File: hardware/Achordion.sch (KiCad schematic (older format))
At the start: 96 parts, among them J1 Power, J10 Jack, J11 Jack, J4 Jack, J5 Jack, J6 Jack, J7 Jack, J8 Jack, J9 Jack, SW2 Button, U4 LM4040C10, U6 TL072, U7 MCP6002, U8 MCP6002, U9 MCP6002

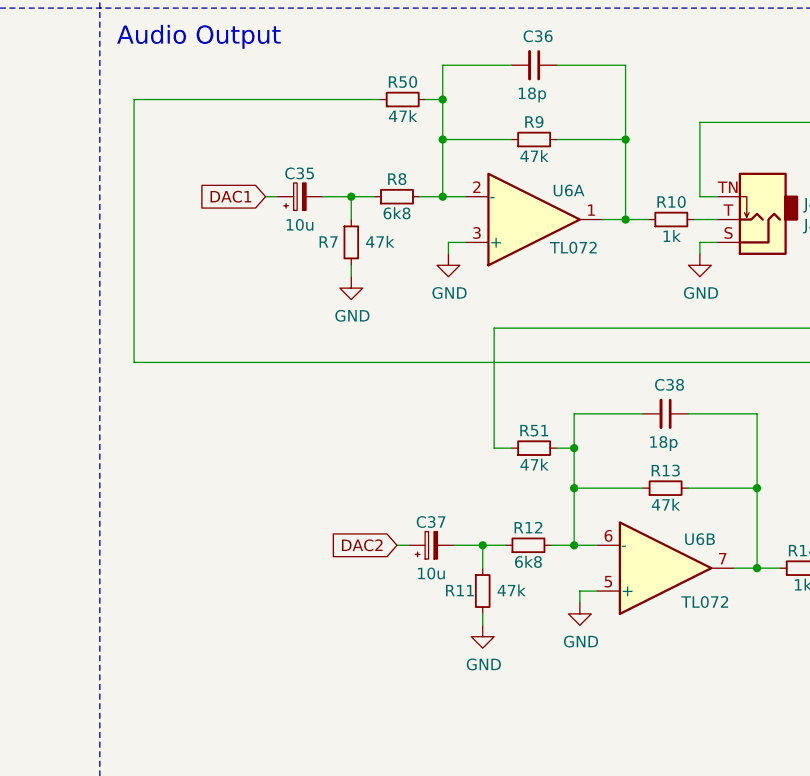
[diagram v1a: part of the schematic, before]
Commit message: Replace DAC decoupling cap with LPF
The design with big decoupling cap was taken from WM8731 used for
Elements. However, with AK4556 used in Daisy Seed, it is not needed (or
at least not a part of the datasheet), instead, use LPF for ~70 kHz.

Signed-off-by: Petr Horacek <hrck@protonmail.com>
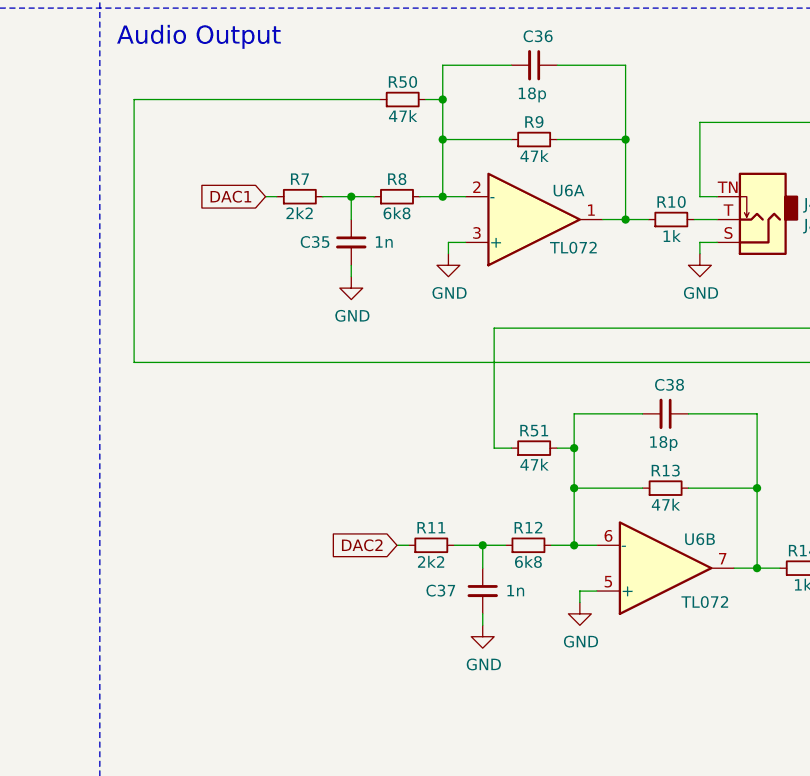
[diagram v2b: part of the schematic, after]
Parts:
- removed C35, C37: 10u, Capacitor_Tantalum_SMD:CP_EIA-3216-18_Kemet-A_Pad1.58x1.35mm_HandSolder, symbol Device:CP_Small
- added C35, C37: 1n, Capacitor_SMD:C_0603_1608Metric_Pad1.08x0.95mm_HandSolder, symbol Device:C_Small
- R11, R7: value 47k -> 2k2; LCSC C25819 -> C23212; Mfr Part Number CR0603-FX-4702ELF -> CR0603-JW-682ELF
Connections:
- net DAC1: now also R7.1
- net DAC2: now also R11.1
- net GND: now also C35.2, C37.2; no longer R11.2, R7.2
- net at R8.1: now also R7.2, C35.1; no longer R7.1
- net at R12.1: now also R11.2, C37.1; no longer R11.1
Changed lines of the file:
@@
 Wire Wire Line
 	13375 7525 13075 7525
-$Comp
-L Device:C_Small C36
-U 1 1 61B7484D
-P 12975 7200
-F 0 "C36" V 12850 7150 50  0000 L CNN
-F 1 "18p" V 13100 7125 50  0000 L CNN
-F 2 "Capacitor_SMD:C_0603_1608Metric_Pad1.08x0.95mm_HandSolder" H 12975 7200 50  0001 C CNN
-F 3 "~" H 12975 7200 50  0001 C CNN
-F 4 "" H 12975 7200 50  0001 C CNN "LCSC Part #"
-F 5 "C1647" H 12975 7200 50  0001 C CNN "LCSC"
-F 6 "1" H 12975 7200 50  0001 C CNN "Order Qty"
-F 7 "CL10C180JB81PNC" H 12975 7200 50  0001 C CNN "Mfr Part Number"
-	1    12975 7200
-	0    1    1    0
-$EndComp
 Wire Wire Line
 	13075 7200 13375 7200
 Wire Wire Line
 	13375 7200 13375 7525
-$Comp
-L Device:R_Small R8
-U 1 1 61BA548D
-P 12375 7775
-F 0 "R8" V 12450 7775 50  0000 C CNN
-F 1 "6k8" V 12300 7775 50  0000 C CNN
-F 2 "Resistor_SMD:R_0603_1608Metric_Pad0.98x0.95mm_HandSolder" H 12375 7775 50  0001 C CNN
-F 3 "~" H 12375 7775 50  0001 C CNN
-F 4 "" H 12375 7775 50  0001 C CNN "LCSC Part #"
-F 5 "C23212 " H 12375 7775 50  0001 C CNN "LCSC"
-F 6 "1" H 12375 7775 50  0001 C CNN "Order Qty"
-F 7 "CR0603-JW-682ELF" H 12375 7775 50  0001 C CNN "Mfr Part Number"
-	1    12375 7775
-	0    -1   -1   0
-$EndComp
 Wire Wire Line
 	12475 7775 12575 7775
@@
 	12600 7975 12675 7975
 $Comp
-L Device:R_Small R7
-U 1 1 61C250CC
-P 12175 7975
-F 0 "R7" H 12075 7975 50  0000 C CNN
-F 1 "47k" H 12300 7975 50  0000 C CNN
-F 2 "Resistor_SMD:R_0603_1608Metric_Pad0.98x0.95mm_HandSolder" H 12175 7975 50  0001 C CNN
-F 3 "~" H 12175 7975 50  0001 C CNN
-F 4 "" H 12175 7975 50  0001 C CNN "LCSC Part #"
-F 5 "C25819" H 12175 7975 50  0001 C CNN "LCSC"
-F 6 "1" H 12175 7975 50  0001 C CNN "Order Qty"
-F 7 "CR0603-FX-4702ELF" H 12175 7975 50  0001 C CNN "Mfr Part Number"
-	1    12175 7975
-	1    0    0    -1
-$EndComp
-$Comp
 L power:GND #PWR051
 U 1 1 61C26EBD
@@
 Wire Wire Line
 	12175 7775 12175 7875
-$Comp
-L Device:CP_Small C35
-U 1 1 61C5FA08
-P 11950 7775
-F 0 "C35" V 12050 7775 50  0000 C CNN
-F 1 "10u" V 11825 7775 50  0000 C CNN
-F 2 "Capacitor_Tantalum_SMD:CP_EIA-3216-18_Kemet-A_Pad1.58x1.35mm_HandSolder" H 11950 7775 50  0001 C CNN
-F 3 "~" H 11950 7775 50  0001 C CNN
-F 4 "" H 11950 7775 50  0001 C CNN "LCSC Part #"
-F 5 "C7171" H 11950 7775 50  0001 C CNN "LCSC"
-F 6 "1" H 11950 7775 50  0001 C CNN "Order Qty"
-F 7 "T491A106K010AT" H 11950 7775 50  0001 C CNN "Mfr Part Number"
-	1    11950 7775
-	0    -1   -1   0
-$EndComp
-Wire Wire Line
-	12050 7775 12175 7775
 Connection ~ 12175 7775
 Wire Wire Line
@@
 Wire Wire Line
 	12750 9300 12750 9400
-$Comp
-L Device:CP_Small C37
-U 1 1 61CD6260
-P 12525 9300
-F 0 "C37" V 12625 9300 50  0000 C CNN
-F 1 "10u" V 12400 9300 50  0000 C CNN
-F 2 "Capacitor_Tantalum_SMD:CP_EIA-3216-18_Kemet-A_Pad1.58x1.35mm_HandSolder" H 12525 9300 50  0001 C CNN
-F 3 "~" H 12525 9300 50  0001 C CNN
-F 4 "" H 12525 9300 50  0001 C CNN "LCSC Part #"
-F 5 "C7171" H 12525 9300 50  0001 C CNN "LCSC"
-F 6 "1" H 12525 9300 50  0001 C CNN "Order Qty"
-F 7 "T491A106K010AT" H 12525 9300 50  0001 C CNN "Mfr Part Number"
-	1    12525 9300
-	0    -1   -1   0
-$EndComp
 Wire Wire Line
 	12625 9300 12750 9300
@@
 Wire Wire Line
 	15750 8475 15750 8425
-$Comp
-L Device:R_Small R11
-U 1 1 61CD6251
-P 12750 9500
-F 0 "R11" H 12650 9500 50  0000 C CNN
-F 1 "47k" H 12875 9500 50  0000 C CNN
-F 2 "Resistor_SMD:R_0603_1608Metric_Pad0.98x0.95mm_HandSolder" H 12750 9500 50  0001 C CNN
-F 3 "~" H 12750 9500 50  0001 C CNN
-F 4 "" H 12750 9500 50  0001 C CNN "LCSC Part #"
-F 5 "C25819" H 12750 9500 50  0001 C CNN "LCSC"
-F 6 "1" H 12750 9500 50  0001 C CNN "Order Qty"
-F 7 "CR0603-FX-4702ELF" H 12750 9500 50  0001 C CNN "Mfr Part Number"
-	1    12750 9500
-	1    0    0    -1
-$EndComp
 Wire Wire Line
 	4250 7475 4350 7475
@@
 Wire Wire Line
 	13650 8725 13950 8725
-$Comp
-L Device:C_Small C38
-U 1 1 61CD6231
-P 13550 8725
-F 0 "C38" V 13425 8675 50  0000 L CNN
-F 1 "18p" V 13675 8650 50  0000 L CNN
-F 2 "Capacitor_SMD:C_0603_1608Metric_Pad1.08x0.95mm_HandSolder" H 13550 8725 50  0001 C CNN
-F 3 "~" H 13550 8725 50  0001 C CNN
-F 4 "" H 13550 8725 50  0001 C CNN "LCSC Part #"
-F 5 "C1647" H 13550 8725 50  0001 C CNN "LCSC"
-F 6 "1" H 13550 8725 50  0001 C CNN "Order Qty"
-F 7 "CL10C180JB81PNC" H 13550 8725 50  0001 C CNN "Mfr Part Number"
-	1    13550 8725
-	0    1    1    0
-$EndComp
 Wire Wire Line
 	13950 9050 13650 9050
@@
 	1    0    0    -1
 $EndComp
+Wire Wire Line
+	12050 7775 12175 7775
+$Comp
+L Device:C_Small C36
+U 1 1 61B7484D
+P 12975 7200
+F 0 "C36" V 12850 7150 50  0000 L CNN
+F 1 "18p" V 13100 7125 50  0000 L CNN
+F 2 "Capacitor_SMD:C_0603_1608Metric_Pad1.08x0.95mm_HandSolder" H 12975 7200 50  0001 C CNN
+F 3 "~" H 12975 7200 50  0001 C CNN
+F 4 "" H 12975 7200 50  0001 C CNN "LCSC Part #"
+F 5 "C1647" H 12975 7200 50  0001 C CNN "LCSC"
+F 6 "1" H 12975 7200 50  0001 C CNN "Order Qty"
+F 7 "CL10C180JB81PNC" H 12975 7200 50  0001 C CNN "Mfr Part Number"
+	1    12975 7200
+	0    1    1    0
+$EndComp
+$Comp
+L Device:C_Small C38
+U 1 1 61CD6231
+P 13550 8725
+F 0 "C38" V 13425 8675 50  0000 L CNN
+F 1 "18p" V 13675 8650 50  0000 L CNN
+F 2 "Capacitor_SMD:C_0603_1608Metric_Pad1.08x0.95mm_HandSolder" H 13550 8725 50  0001 C CNN
+F 3 "~" H 13550 8725 50  0001 C CNN
+F 4 "" H 13550 8725 50  0001 C CNN "LCSC Part #"
+F 5 "C1647" H 13550 8725 50  0001 C CNN "LCSC"
+F 6 "1" H 13550 8725 50  0001 C CNN "Order Qty"
+F 7 "CL10C180JB81PNC" H 13550 8725 50  0001 C CNN "Mfr Part Number"
+	1    13550 8725
+	0    1    1    0
+$EndComp
+$Comp
+L Device:R_Small R8
+U 1 1 61BA548D
+P 12375 7775
+F 0 "R8" V 12450 7775 50  0000 C CNN
+F 1 "6k8" V 12300 7775 50  0000 C CNN
+F 2 "Resistor_SMD:R_0603_1608Metric_Pad0.98x0.95mm_HandSolder" H 12375 7775 50  0001 C CNN
+F 3 "~" H 12375 7775 50  0001 C CNN
+F 4 "" H 12375 7775 50  0001 C CNN "LCSC Part #"
+F 5 "C23212 " H 12375 7775 50  0001 C CNN "LCSC"
+F 6 "1" H 12375 7775 50  0001 C CNN "Order Qty"
+F 7 "CR0603-JW-682ELF" H 12375 7775 50  0001 C CNN "Mfr Part Number"
+	1    12375 7775
+	0    -1   -1   0
+$EndComp
+$Comp
+L Device:C_Small C35
+U 1 1 610A838E
+P 12175 7975
+F 0 "C35" H 11950 7975 50  0000 L CNN
+F 1 "1n" H 12275 7975 50  0000 L CNN
+F 2 "Capacitor_SMD:C_0603_1608Metric_Pad1.08x0.95mm_HandSolder" H 12175 7975 50  0001 C CNN
+F 3 "~" H 12175 7975 50  0001 C CNN
+F 4 "" H 12175 7975 50  0001 C CNN "LCSC Part #"
+F 5 "C14663" H 12175 7975 50  0001 C CNN "LCSC"
+F 6 "1" H 12175 7975 50  0001 C CNN "Order Qty"
+F 7 "CL10F104ZO8NNNC" H 12175 7975 50  0001 C CNN "Mfr Part Number"
+	1    12175 7975
+	1    0    0    -1
+$EndComp
+$Comp
+L Device:R_Small R7
+U 1 1 610E59C7
+P 11950 7775
+F 0 "R7" V 12025 7775 50  0000 C CNN
+F 1 "2k2" V 11875 7775 50  0000 C CNN
+F 2 "Resistor_SMD:R_0603_1608Metric_Pad0.98x0.95mm_HandSolder" H 11950 7775 50  0001 C CNN
+F 3 "~" H 11950 7775 50  0001 C CNN
+F 4 "" H 11950 7775 50  0001 C CNN "LCSC Part #"
+F 5 "C23212 " H 11950 7775 50  0001 C CNN "LCSC"
+F 6 "1" H 11950 7775 50  0001 C CNN "Order Qty"
+F 7 "CR0603-JW-682ELF" H 11950 7775 50  0001 C CNN "Mfr Part Number"
+	1    11950 7775
+	0    -1   -1   0
+$EndComp
+$Comp
+L Device:C_Small C37
+U 1 1 610B25D6
+P 12750 9500
+F 0 "C37" H 12500 9500 50  0000 L CNN
+F 1 "1n" H 12850 9500 50  0000 L CNN
+F 2 "Capacitor_SMD:C_0603_1608Metric_Pad1.08x0.95mm_HandSolder" H 12750 9500 50  0001 C CNN
+F 3 "~" H 12750 9500 50  0001 C CNN
+F 4 "" H 12750 9500 50  0001 C CNN "LCSC Part #"
+F 5 "C14663" H 12750 9500 50  0001 C CNN "LCSC"
+F 6 "1" H 12750 9500 50  0001 C CNN "Order Qty"
+F 7 "CL10F104ZO8NNNC" H 12750 9500 50  0001 C CNN "Mfr Part Number"
+	1    12750 9500
+	1    0    0    -1
+$EndComp
+$Comp
+L Device:R_Small R11
+U 1 1 6110D116
+P 12525 9300
+F 0 "R11" V 12600 9300 50  0000 C CNN
+F 1 "2k2" V 12450 9300 50  0000 C CNN
+F 2 "Resistor_SMD:R_0603_1608Metric_Pad0.98x0.95mm_HandSolder" H 12525 9300 50  0001 C CNN
+F 3 "~" H 12525 9300 50  0001 C CNN
+F 4 "" H 12525 9300 50  0001 C CNN "LCSC Part #"
+F 5 "C23212 " H 12525 9300 50  0001 C CNN "LCSC"
+F 6 "1" H 12525 9300 50  0001 C CNN "Order Qty"
+F 7 "CR0603-JW-682ELF" H 12525 9300 50  0001 C CNN "Mfr Part Number"
+	1    12525 9300
+	0    -1   -1   0
+$EndComp
 $EndSCHEMATC

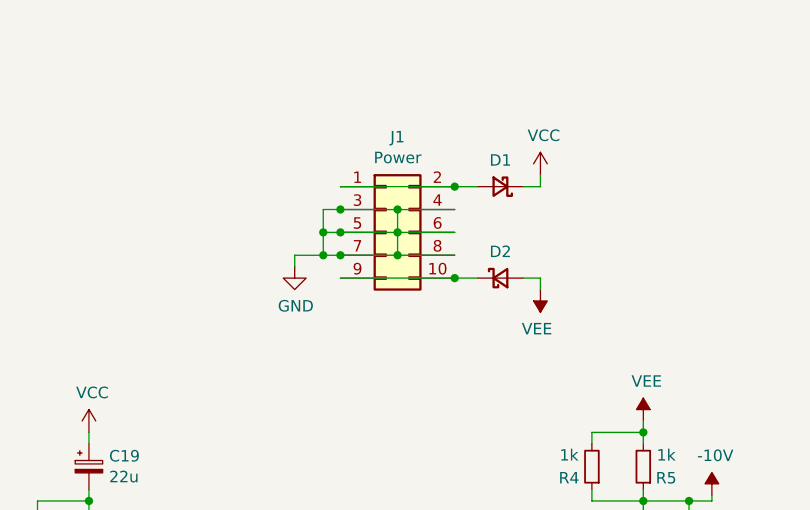
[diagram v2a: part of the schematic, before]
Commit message: Add ferrite bead to filter power input
Signed-off-by: Petr Horacek <hrck@protonmail.com>
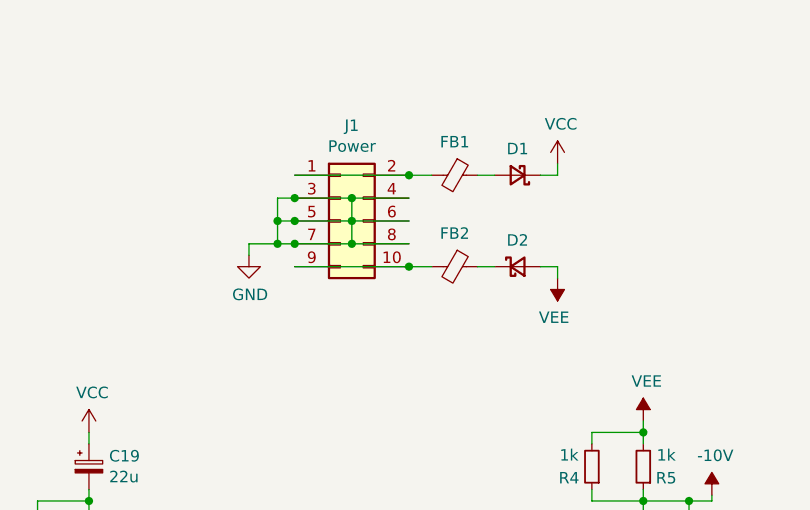
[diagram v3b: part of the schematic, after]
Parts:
- added FB1, FB2: Ferrite_Bead_Small, Inductor_SMD:L_0603_1608Metric_Pad1.05x0.95mm_HandSolder, symbol Device:Ferrite_Bead_Small
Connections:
- net at J1.1 (Pin_1), J1.2 (Pin_2): now also FB1.2; no longer D1.2 (A)
- net at J1.10 (Pin_10), J1.9 (Pin_9): now also FB2.2; no longer D2.1 (K)
- new net: D1.2 (A), FB1.1
- new net: D2.1 (K), FB2.1
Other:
- moved on the sheet: D1, D2, J1
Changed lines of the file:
@@
 L Device:D_Schottky_Small D1
 U 1 1 60A7F779
-P 14075 1225
-F 0 "D1" H 14075 1110 50  0000 C CNN
-F 1 "D_Schottky_Small" H 14075 1109 50  0001 C CNN
-F 2 "Diode_SMD:D_SOD-123" V 14075 1225 50  0001 C CNN
-F 3 "" V 14075 1225 50  0001 C CNN
-F 4 "" H 14075 1225 50  0001 C CNN "LCSC Part #"
-F 5 "C8598" H 14075 1225 50  0001 C CNN "LCSC"
-F 6 "STPS0540ZY" H 14075 1225 50  0001 C CNN "Mfr Part Number"
-F 7 "1" H 14075 1225 50  0001 C CNN "Order Qty"
-	1    14075 1225
+P 14150 1175
+F 0 "D1" H 14150 1060 50  0000 C CNN
+F 1 "D_Schottky_Small" H 14150 1059 50  0001 C CNN
+F 2 "Diode_SMD:D_SOD-123" V 14150 1175 50  0001 C CNN
+F 3 "" V 14150 1175 50  0001 C CNN
+F 4 "" H 14150 1175 50  0001 C CNN "LCSC Part #"
+F 5 "C8598" H 14150 1175 50  0001 C CNN "LCSC"
+F 6 "STPS0540ZY" H 14150 1175 50  0001 C CNN "Mfr Part Number"
+F 7 "1" H 14150 1175 50  0001 C CNN "Order Qty"
+	1    14150 1175
 	-1   0    0    1
 $EndComp
@@
 L Device:D_Schottky_Small D2
 U 1 1 60A9369C
-P 14075 1625
-F 0 "D2" H 14075 1740 50  0000 C CNN
-F 1 "D_Schottky_Small" H 14075 1509 50  0001 C CNN
-F 2 "Diode_SMD:D_SOD-123" V 14075 1625 50  0001 C CNN
-F 3 "" V 14075 1625 50  0001 C CNN
-F 4 "" H 14075 1625 50  0001 C CNN "LCSC Part #"
-F 5 "C8598" H 14075 1625 50  0001 C CNN "LCSC"
-F 6 "STPS0540ZY" H 14075 1625 50  0001 C CNN "Mfr Part Number"
-F 7 "1" H 14075 1625 50  0001 C CNN "Order Qty"
-	1    14075 1625
+P 14150 1575
+F 0 "D2" H 14150 1690 50  0000 C CNN
+F 1 "D_Schottky_Small" H 14150 1459 50  0001 C CNN
+F 2 "Diode_SMD:D_SOD-123" V 14150 1575 50  0001 C CNN
+F 3 "" V 14150 1575 50  0001 C CNN
+F 4 "" H 14150 1575 50  0001 C CNN "LCSC Part #"
+F 5 "C8598" H 14150 1575 50  0001 C CNN "LCSC"
+F 6 "STPS0540ZY" H 14150 1575 50  0001 C CNN "Mfr Part Number"
+F 7 "1" H 14150 1575 50  0001 C CNN "Order Qty"
+	1    14150 1575
 	1    0    0    -1
 $EndComp
@@
 L power:VCC #PWR036
 U 1 1 60A9A4CE
-P 14250 1175
-F 0 "#PWR036" H 14250 1025 50  0001 C CNN
-F 1 "VCC" H 14265 1348 50  0000 C CNN
-F 2 "" H 14250 1175 50  0001 C CNN
-F 3 "" H 14250 1175 50  0001 C CNN
-	1    14250 1175
+P 14325 1125
+F 0 "#PWR036" H 14325 975 50  0001 C CNN
+F 1 "VCC" H 14340 1298 50  0000 C CNN
+F 2 "" H 14325 1125 50  0001 C CNN
+F 3 "" H 14325 1125 50  0001 C CNN
+	1    14325 1125
 	1    0    0    -1
 $EndComp
@@
 L power:VEE #PWR037
 U 1 1 60A9B148
-P 14250 1675
-F 0 "#PWR037" H 14250 1525 50  0001 C CNN
-F 1 "VEE" H 14265 1848 50  0000 C CNN
-F 2 "" H 14250 1675 50  0001 C CNN
-F 3 "" H 14250 1675 50  0001 C CNN
-	1    14250 1675
+P 14325 1625
+F 0 "#PWR037" H 14325 1475 50  0001 C CNN
+F 1 "VEE" H 14340 1798 50  0000 C CNN
+F 2 "" H 14325 1625 50  0001 C CNN
+F 3 "" H 14325 1625 50  0001 C CNN
+	1    14325 1625
 	-1   0    0    1
 $EndComp
 Wire Wire Line
-	14250 1675 14250 1625
-Wire Wire Line
-	14250 1625 14175 1625
-Wire Wire Line
-	14250 1175 14250 1225
-Wire Wire Line
-	14250 1225 14175 1225
-Wire Wire Line
-	13300 1525 13175 1525
-Wire Wire Line
-	13175 1525 13175 1575
+	14325 1625 14325 1575
+Wire Wire Line
+	14325 1575 14250 1575
+Wire Wire Line
+	14325 1125 14325 1175
+Wire Wire Line
+	14325 1175 14250 1175
+Wire Wire Line
+	13100 1475 12975 1475
+Wire Wire Line
+	12975 1475 12975 1525
 $Comp
 L power:GND #PWR026
 U 1 1 60A7877E
-P 13175 1575
-F 0 "#PWR026" H 13175 1325 50  0001 C CNN
-F 1 "GND" H 13180 1402 50  0000 C CNN
-F 2 "" H 13175 1575 50  0001 C CNN
-F 3 "" H 13175 1575 50  0001 C CNN
-	1    13175 1575
-	1    0    0    -1
-$EndComp
-Connection ~ 13300 1525
-Wire Wire Line
-	13300 1325 13300 1425
-Wire Wire Line
-	13300 1425 13300 1525
-Connection ~ 13300 1425
-Wire Wire Line
-	13625 1325 13625 1425
-Connection ~ 13625 1325
-Wire Wire Line
-	13625 1325 13875 1325
-Connection ~ 13625 1425
-Wire Wire Line
-	13625 1425 13875 1425
-Wire Wire Line
-	13625 1425 13625 1525
-Wire Wire Line
-	13875 1525 13625 1525
-Connection ~ 13625 1525
-Wire Wire Line
-	13300 1525 13375 1525
-Wire Wire Line
-	13625 1525 13375 1525
-Connection ~ 13375 1525
-Wire Wire Line
-	13375 1425 13625 1425
-Wire Wire Line
-	13375 1425 13300 1425
-Connection ~ 13375 1425
-Wire Wire Line
-	13375 1325 13625 1325
-Wire Wire Line
-	13375 1325 13300 1325
-Connection ~ 13375 1325
-Wire Wire Line
-	13875 1225 13975 1225
-Wire Wire Line
-	13875 1225 13375 1225
-Connection ~ 13875 1225
-Wire Wire Line
-	13875 1625 13975 1625
-Wire Wire Line
-	13375 1625 13875 1625
-Connection ~ 13875 1625
+P 12975 1525
+F 0 "#PWR026" H 12975 1275 50  0001 C CNN
+F 1 "GND" H 12980 1352 50  0000 C CNN
+F 2 "" H 12975 1525 50  0001 C CNN
+F 3 "" H 12975 1525 50  0001 C CNN
+	1    12975 1525
+	1    0    0    -1
+$EndComp
+Connection ~ 13100 1475
+Wire Wire Line
+	13100 1275 13100 1375
+Wire Wire Line
+	13100 1375 13100 1475
+Connection ~ 13100 1375
+Wire Wire Line
+	13425 1275 13425 1375
+Connection ~ 13425 1275
+Wire Wire Line
+	13425 1275 13675 1275
+Connection ~ 13425 1375
+Wire Wire Line
+	13425 1375 13675 1375
+Wire Wire Line
+	13425 1375 13425 1475
+Wire Wire Line
+	13675 1475 13425 1475
+Connection ~ 13425 1475
+Wire Wire Line
+	13100 1475 13175 1475
+Wire Wire Line
+	13425 1475 13175 1475
+Connection ~ 13175 1475
+Wire Wire Line
+	13175 1375 13425 1375
+Wire Wire Line
+	13175 1375 13100 1375
+Connection ~ 13175 1375
+Wire Wire Line
+	13175 1275 13425 1275
+Wire Wire Line
+	13175 1275 13100 1275
+Connection ~ 13175 1275
+Wire Wire Line
+	13675 1175 13775 1175
+Wire Wire Line
+	13675 1175 13175 1175
+Connection ~ 13675 1175
+Wire Wire Line
+	13675 1575 13775 1575
+Wire Wire Line
+	13175 1575 13675 1575
+Connection ~ 13675 1575
 $Comp
 L Connector_Generic:Conn_02x05_Odd_Even J1
 U 1 1 60A5352E
-P 13575 1425
-F 0 "J1" H 13625 1842 50  0000 C CNN
-F 1 "Power" H 13625 1751 50  0000 C CNN
-F 2 "Connector_PinHeader_2.54mm:PinHeader_2x05_P2.54mm_Vertical" H 13575 1425 50  0001 C CNN
-F 3 "" H 13575 1425 50  0001 C CNN
-F 4 "87914-1016" H 13575 1425 50  0001 C CNN "Mfr Part Number"
-F 5 "1" H 13575 1425 50  0001 C CNN "Order Qty"
-	1    13575 1425
+P 13375 1375
+F 0 "J1" H 13425 1792 50  0000 C CNN
+F 1 "Power" H 13425 1701 50  0000 C CNN
+F 2 "Connector_PinHeader_2.54mm:PinHeader_2x05_P2.54mm_Vertical" H 13375 1375 50  0001 C CNN
+F 3 "" H 13375 1375 50  0001 C CNN
+F 4 "87914-1016" H 13375 1375 50  0001 C CNN "Mfr Part Number"
+F 5 "1" H 13375 1375 50  0001 C CNN "Order Qty"
+	1    13375 1375
 	1    0    0    -1
 $EndComp
@@
 	0    -1   -1   0
 $EndComp
+$Comp
+L Device:Ferrite_Bead_Small FB1
+U 1 1 611CC9CE
+P 13875 1175
+F 0 "FB1" V 13730 1175 50  0000 C CNN
+F 1 "Ferrite_Bead_Small" V 13729 1175 50  0001 C CNN
+F 2 "Inductor_SMD:L_0603_1608Metric_Pad1.05x0.95mm_HandSolder" V 13805 1175 50  0001 C CNN
+F 3 "~" H 13875 1175 50  0001 C CNN
+	1    13875 1175
+	0    1    1    0
+$EndComp
+$Comp
+L Device:Ferrite_Bead_Small FB2
+U 1 1 611CCF5E
+P 13875 1575
+F 0 "FB2" V 13730 1575 50  0000 C CNN
+F 1 "Ferrite_Bead_Small" V 13729 1575 50  0001 C CNN
+F 2 "Inductor_SMD:L_0603_1608Metric_Pad1.05x0.95mm_HandSolder" V 13805 1575 50  0001 C CNN
+F 3 "~" H 13875 1575 50  0001 C CNN
+	1    13875 1575
+	0    1    1    0
+$EndComp
+Wire Wire Line
+	14050 1175 13975 1175
+Wire Wire Line
+	13975 1575 14050 1575
 $EndSCHEMATC

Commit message: Replace tantalum DC decoupling caps with aluminium
Tantalum has some bad stories connected with it. This patch replaces
them with bigger, but much more common aluminium capacitors.

Signed-off-by: Petr Horacek <hrck@protonmail.com>
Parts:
- C19, C20: footprint Capacitor_Tantalum_SMD:CP_EIA-3528-21_Kemet-B_Pad1.50x2.35mm_HandSolder -> Capacitor_SMD:CP_Elec_6.3x5.8
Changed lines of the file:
@@
 F 0 "C20" H 12363 2796 50  0000 L CNN
 F 1 "22u" H 12363 2705 50  0000 L CNN
-F 2 "Capacitor_Tantalum_SMD:CP_EIA-3528-21_Kemet-B_Pad1.50x2.35mm_HandSolder" H 12275 2750 50  0001 C CNN
+F 2 "Capacitor_SMD:CP_Elec_6.3x5.8" H 12275 2750 50  0001 C CNN
 F 3 "~" H 12275 2750 50  0001 C CNN
 F 4 "" H 12275 2750 50  0001 C CNN "LCSC Part #"
@@
 F 0 "C19" H 12363 2496 50  0000 L CNN
 F 1 "22u" H 12363 2405 50  0000 L CNN
-F 2 "Capacitor_Tantalum_SMD:CP_EIA-3528-21_Kemet-B_Pad1.50x2.35mm_HandSolder" H 12275 2450 50  0001 C CNN
+F 2 "Capacitor_SMD:CP_Elec_6.3x5.8" H 12275 2450 50  0001 C CNN
 F 3 "~" H 12275 2450 50  0001 C CNN
 F 4 "" H 12275 2450 50  0001 C CNN "LCSC Part #"
